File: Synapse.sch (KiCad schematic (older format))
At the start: 5 parts, among them U1 WeAct_BlackPill

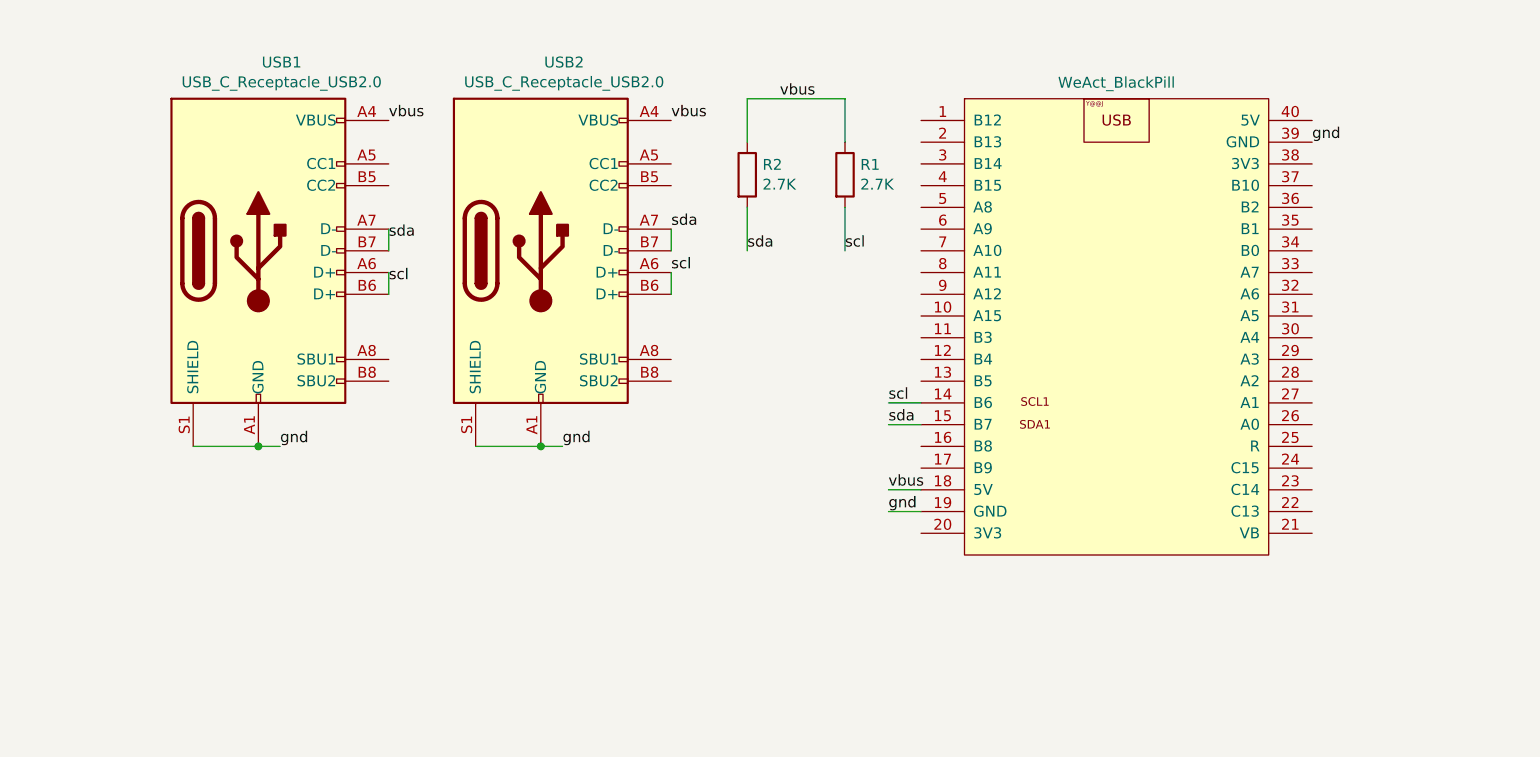
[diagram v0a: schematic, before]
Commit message: Rebuild the pcb in a cleaner way
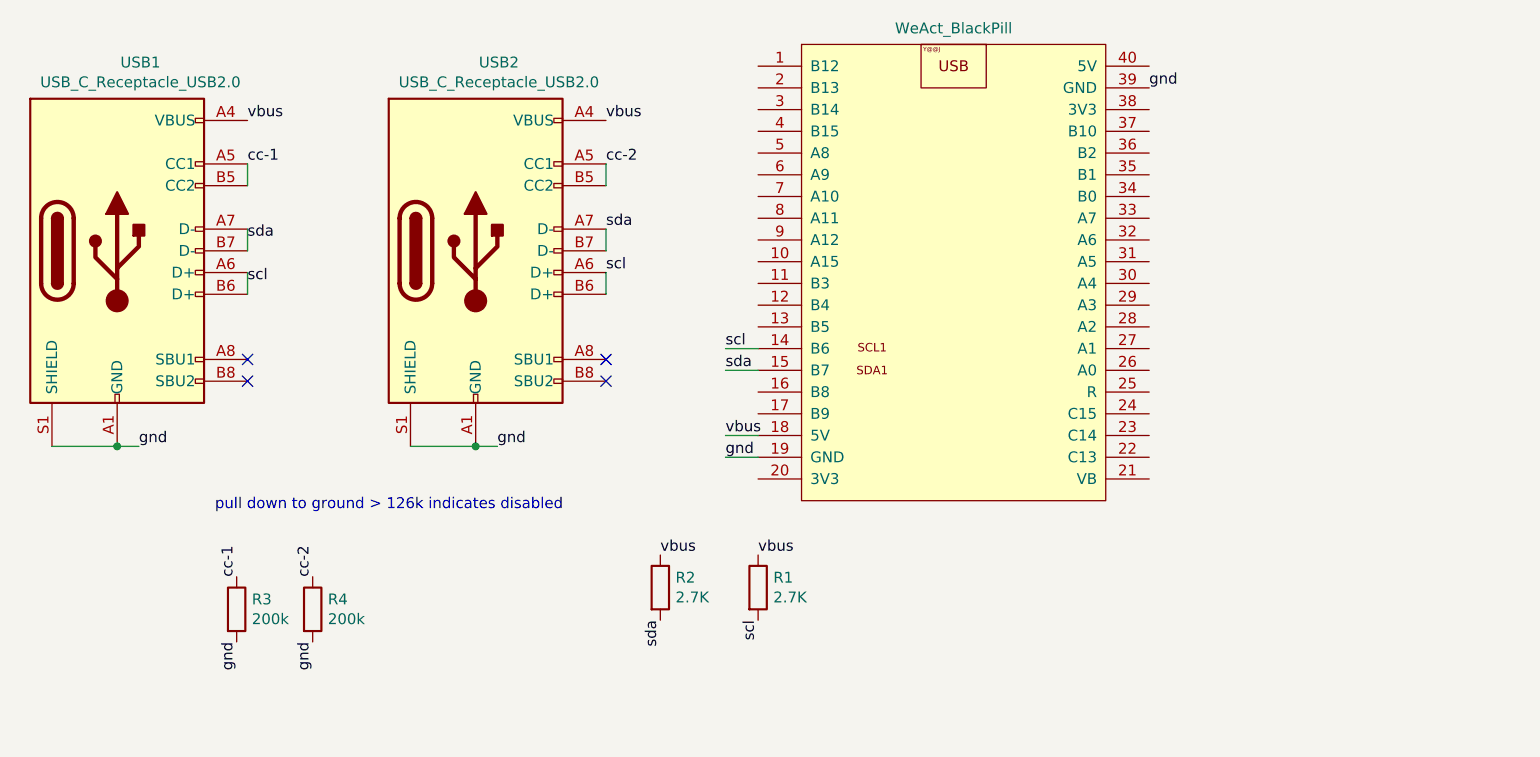
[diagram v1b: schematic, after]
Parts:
- added R3, R4: 200k, Resistor_SMD:R_1206_3216Metric, symbol Device:R
- R1, R2: LCSC (none) -> C17950
- USB1, USB2: LCSC (none) -> C165948
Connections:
- net gnd: now also R3.2, R4.2
- net cc-2: now reaches USB2.A5 (CC1)
- net cc-2: now also USB2.B5 (CC2), R4.1
- net cc-1: now reaches USB1.A5 (CC1)
- net cc-1: now also USB1.B5 (CC2), R3.1
- no-connect marks 0 -> 4
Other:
- note added: "pull down to ground > 126k indicates disabled"
- moved on the sheet: R1, R2, USB1, USB2
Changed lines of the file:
@@
 L Device:R R1
 U 1 1 60F04B0D
-P 6350 1850
-F 0 "R1" H 6420 1896 50  0000 L CNN
-F 1 "2.7K" H 6420 1805 50  0000 L CNN
-F 2 "Resistor_SMD:R_1206_3216Metric" V 6280 1850 50  0001 C CNN
-F 3 "~" H 6350 1850 50  0001 C CNN
-	1    6350 1850
-	1    0    0    -1
-$EndComp
-$Comp
-L Device:R R2
-U 1 1 60F0593A
-P 5900 1850
-F 0 "R2" H 5970 1896 50  0000 L CNN
-F 1 "2.7K" H 5970 1805 50  0000 L CNN
-F 2 "Resistor_SMD:R_1206_3216Metric" V 5830 1850 50  0001 C CNN
-F 3 "~" H 5900 1850 50  0001 C CNN
-	1    5900 1850
+P 5950 3750
+F 0 "R1" H 6020 3796 50  0000 L CNN
+F 1 "2.7K" H 6020 3705 50  0000 L CNN
+F 2 "Resistor_SMD:R_1206_3216Metric" V 5880 3750 50  0001 C CNN
+F 3 "~" H 5950 3750 50  0001 C CNN
+F 4 "C17950" H 5950 3750 50  0001 C CNN "LCSC"
+	1    5950 3750
 	1    0    0    -1
 $EndComp
 Wire Wire Line
-	6700 3400 6550 3400
+	5950 3150 5800 3150
 $Comp
 L Connector:USB_C_Receptacle_USB2.0 USB1
 U 1 1 60F0D514
-P 3650 2200
-F 0 "USB1" H 3757 3067 50  0000 C CNN
-F 1 "USB_C_Receptacle_USB2.0" H 3757 2976 50  0000 C CNN
-F 2 "Connector_USB:USB_C_Receptacle_HRO_TYPE-C-31-M-12" H 3800 2200 50  0001 C CNN
-F 3 "https://www.usb.org/sites/default/files/documents/usb_type-c.zip" H 3800 2200 50  0001 C CNN
-	1    3650 2200
+P 3000 2200
+F 0 "USB1" H 3107 3067 50  0000 C CNN
+F 1 "USB_C_Receptacle_USB2.0" H 3107 2976 50  0000 C CNN
+F 2 "Connector_USB:USB_C_Receptacle_HRO_TYPE-C-31-M-12" H 3150 2200 50  0001 C CNN
+F 3 "https://www.usb.org/sites/default/files/documents/usb_type-c.zip" H 3150 2200 50  0001 C CNN
+F 4 "C165948" H 3000 2200 50  0001 C CNN "LCSC"
+	1    3000 2200
 	1    0    0    -1
 $EndComp
 Wire Wire Line
-	5550 2100 5550 2200
+	5250 2100 5250 2200
 Wire Wire Line
-	4650 3100 4950 3100
-Connection ~ 4950 3100
+	4350 3100 4650 3100
+Connection ~ 4650 3100
 Wire Wire Line
-	3350 3100 3650 3100
-Text Label 6550 3400 0    50   ~ 0
+	2700 3100 3000 3100
+Text Label 5800 3150 0    50   ~ 0
 gnd
-Text Label 6550 3300 0    50   ~ 0
+Text Label 5800 3050 0    50   ~ 0
 vbus
-Text Label 8500 1700 0    50   ~ 0
+Text Label 7750 1450 0    50   ~ 0
 gnd
-Text Label 5550 2100 0    50   ~ 0
+Text Label 5250 2100 0    50   ~ 0
 sda
-Text Label 6550 3000 0    50   ~ 0
+Text Label 5800 2750 0    50   ~ 0
 sda
-Text Label 6050 1500 0    50   ~ 0
+Text Label 5250 1600 0    50   ~ 0
 vbus
+Text Label 5950 3900 3    50   ~ 0
+scl
+Text Label 5800 2650 0    50   ~ 0
+scl
 Wire Wire Line
-	5900 1500 5900 1700
+	5800 2650 5950 2650
 Wire Wire Line
-	6350 1500 6350 1700
+	5800 3050 5950 3050
+Text Label 4750 3100 0    50   ~ 0
+gnd
 Wire Wire Line
-	5900 1500 6350 1500
-Text Label 5550 1600 0    50   ~ 0
-vbus
-Text Label 5900 2200 0    50   ~ 0
+	4650 3100 4750 3100
+Text Label 3100 3100 0    50   ~ 0
+gnd
+Wire Wire Line
+	3000 3100 3100 3100
+Connection ~ 3000 3100
+Text Label 3600 2150 0    50   ~ 0
 sda
 Wire Wire Line
-	5900 2200 5900 2000
-Text Label 6350 2200 0    50   ~ 0
+	3600 2100 3600 2200
+Wire Wire Line
+	5950 2750 5800 2750
+Text Label 3600 2350 0    50   ~ 0
 scl
 Wire Wire Line
-	6350 2200 6350 2000
-Text Label 6550 2900 0    50   ~ 0
+	3600 2300 3600 2400
+Text Label 5250 2300 0    50   ~ 0
 scl
-Wire Wire Line
-	6550 2900 6700 2900
-Wire Wire Line
-	6550 3300 6700 3300
-Text Label 5050 3100 0    50   ~ 0
-gnd
-Wire Wire Line
-	4950 3100 5050 3100
-Text Label 3750 3100 0    50   ~ 0
-gnd
-Wire Wire Line
-	3650 3100 3750 3100
-Connection ~ 3650 3100
-Text Label 4250 2150 0    50   ~ 0
-sda
-Wire Wire Line
-	4250 2100 4250 2200
-Wire Wire Line
-	6700 3000 6550 3000
-Text Label 4250 2350 0    50   ~ 0
-scl
-Wire Wire Line
-	4250 2300 4250 2400
-Text Label 5550 2300 0    50   ~ 0
-scl
-Text Label 4250 1600 0    50   ~ 0
+Text Label 3600 1600 0    50   ~ 0
 vbus
 $Comp
 L Connector:USB_C_Receptacle_USB2.0 USB2
 U 1 1 60F06A9E
-P 4950 2200
-F 0 "USB2" H 5057 3067 50  0000 C CNN
-F 1 "USB_C_Receptacle_USB2.0" H 5057 2976 50  0000 C CNN
-F 2 "Connector_USB:USB_C_Receptacle_HRO_TYPE-C-31-M-12" H 5100 2200 50  0001 C CNN
-F 3 "https://www.usb.org/sites/default/files/documents/usb_type-c.zip" H 5100 2200 50  0001 C CNN
-	1    4950 2200
+P 4650 2200
+F 0 "USB2" H 4757 3067 50  0000 C CNN
+F 1 "USB_C_Receptacle_USB2.0" H 4757 2976 50  0000 C CNN
+F 2 "Connector_USB:USB_C_Receptacle_HRO_TYPE-C-31-M-12" H 4800 2200 50  0001 C CNN
+F 3 "https://www.usb.org/sites/default/files/documents/usb_type-c.zip" H 4800 2200 50  0001 C CNN
+F 4 "C165948" H 4650 2200 50  0001 C CNN "LCSC"
+	1    4650 2200
 	1    0    0    -1
 $EndComp
 Wire Wire Line
-	5550 2400 5550 2300
+	5250 2400 5250 2300
 $Comp
 L YAAJ_BlackPill:WeAct_BlackPill U1
 U 1 1 60EFFF91
-P 7600 2500
-F 0 "U1" H 7600 3665 50  0001 C CNN
-F 1 "WeAct_BlackPill" H 7600 3574 50  0000 C CNN
-F 2 "Footprints:YAAJ_BluePill_2" H 8400 1500 50  0001 C CNN
-F 3 "" H 8400 1500 50  0001 C CNN
-	1    7600 2500
+P 6850 2250
+F 0 "U1" H 6850 3415 50  0001 C CNN
+F 1 "WeAct_BlackPill" H 6850 3324 50  0000 C CNN
+F 2 "Footprints:YAAJ_BluePill_2" H 7650 1250 50  0001 C CNN
+F 3 "" H 7650 1250 50  0001 C CNN
+	1    6850 2250
 	1    0    0    -1
 $EndComp
+NoConn ~ 5250 2700
+NoConn ~ 5250 2800
+NoConn ~ 3600 2700
+NoConn ~ 3600 2800
+$Comp
+L Device:R R4
+U 1 1 60F1AE6D
+P 3900 3850
+F 0 "R4" H 3970 3896 50  0000 L CNN
+F 1 "200k" H 3970 3805 50  0000 L CNN
+F 2 "Resistor_SMD:R_1206_3216Metric" V 3830 3850 50  0001 C CNN
+F 3 "~" H 3900 3850 50  0001 C CNN
+F 4 "C17954" H 3900 3850 50  0001 C CNN "LCSC"
+	1    3900 3850
+	1    0    0    -1
+$EndComp
+Text Label 5950 3600 0    50   ~ 0
+vbus
+Text Label 5500 3900 3    50   ~ 0
+sda
+Text Label 5500 3600 0    50   ~ 0
+vbus
+$Comp
+L Device:R R2
+U 1 1 60F0593A
+P 5500 3750
+F 0 "R2" H 5570 3796 50  0000 L CNN
+F 1 "2.7K" H 5570 3705 50  0000 L CNN
+F 2 "Resistor_SMD:R_1206_3216Metric" V 5430 3750 50  0001 C CNN
+F 3 "~" H 5500 3750 50  0001 C CNN
+F 4 "C17950" H 5500 3750 50  0001 C CNN "LCSC"
+	1    5500 3750
+	1    0    0    -1
+$EndComp
+Text Label 3550 3700 1    50   ~ 0
+cc-1
+$Comp
+L Device:R R3
+U 1 1 60F1A5DE
+P 3550 3850
+F 0 "R3" H 3620 3896 50  0000 L CNN
+F 1 "200k" H 3620 3805 50  0000 L CNN
+F 2 "Resistor_SMD:R_1206_3216Metric" V 3480 3850 50  0001 C CNN
+F 3 "~" H 3550 3850 50  0001 C CNN
+F 4 "C17954" H 3550 3850 50  0001 C CNN "LCSC"
+	1    3550 3850
+	1    0    0    -1
+$EndComp
+Text Label 3900 3700 1    50   ~ 0
+cc-2
+Text Notes 3450 3400 0    50   ~ 0
+pull down to ground > 126k indicates disabled
+Text Label 3600 1800 0    50   ~ 0
+cc-1
+Wire Wire Line
+	3600 1800 3600 1900
+Text Label 5250 1800 0    50   ~ 0
+cc-2
+Wire Wire Line
+	5250 1800 5250 1900
+Text Label 3550 4000 3    50   ~ 0
+gnd
+Text Label 3900 4000 3    50   ~ 0
+gnd
 $EndSCHEMATC

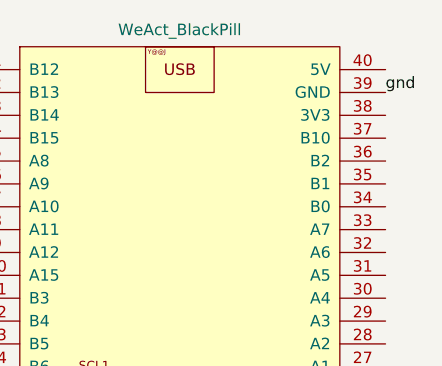
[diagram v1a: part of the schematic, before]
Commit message: Use VCC for a top layer
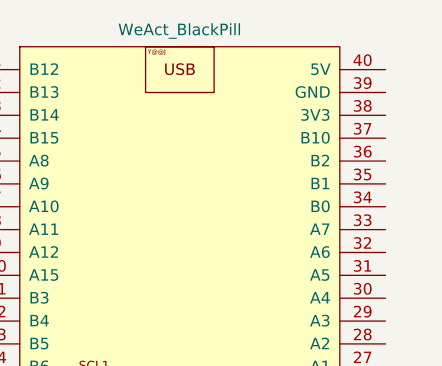
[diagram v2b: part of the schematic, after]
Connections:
- net gnd: no longer U1.39 (GND)
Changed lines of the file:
@@
 Text Label 5800 3050 0    50   ~ 0
 vbus
-Text Label 7750 1450 0    50   ~ 0
-gnd
 Text Label 5250 2100 0    50   ~ 0
 sda

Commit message: synapse mini
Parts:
- removed U1: WeAct_BlackPill, Footprints:YAAJ_BluePill_2, symbol YAAJ_BlackPill:WeAct_BlackPill
- added U2: WeAct_BlackPill_Short, Footprints:BlackPill_Short, symbol YAAJ_BlackPill:WeAct_BlackPill_Short
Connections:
- wire segments 14 -> 18
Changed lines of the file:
@@
 	1    0    0    -1
 $EndComp
-Wire Wire Line
-	5950 3150 5800 3150
 $Comp
 L Connector:USB_C_Receptacle_USB2.0 USB1
@@
 Wire Wire Line
 	2700 3100 3000 3100
-Text Label 5800 3150 0    50   ~ 0
+Text Label 5750 2150 2    50   ~ 0
 gnd
-Text Label 5800 3050 0    50   ~ 0
+Text Label 5750 2050 2    50   ~ 0
 vbus
 Text Label 5250 2100 0    50   ~ 0
 sda
-Text Label 5800 2750 0    50   ~ 0
+Text Label 5750 1750 2    50   ~ 0
 sda
 Text Label 5250 1600 0    50   ~ 0
@@
 Text Label 5950 3900 3    50   ~ 0
 scl
-Text Label 5800 2650 0    50   ~ 0
+Text Label 5750 1650 2    50   ~ 0
 scl
-Wire Wire Line
-	5800 2650 5950 2650
-Wire Wire Line
-	5800 3050 5950 3050
 Text Label 4750 3100 0    50   ~ 0
 gnd
@@
 Wire Wire Line
 	3600 2100 3600 2200
-Wire Wire Line
-	5950 2750 5800 2750
 Text Label 3600 2350 0    50   ~ 0
 scl
@@
 Wire Wire Line
 	5250 2400 5250 2300
-$Comp
-L YAAJ_BlackPill:WeAct_BlackPill U1
-U 1 1 60EFFF91
-P 6850 2250
-F 0 "U1" H 6850 3415 50  0001 C CNN
-F 1 "WeAct_BlackPill" H 6850 3324 50  0000 C CNN
-F 2 "Footprints:YAAJ_BluePill_2" H 7650 1250 50  0001 C CNN
-F 3 "" H 7650 1250 50  0001 C CNN
-	1    6850 2250
-	1    0    0    -1
-$EndComp
 NoConn ~ 5250 2700
 NoConn ~ 5250 2800
@@
 Text Label 3900 4000 3    50   ~ 0
 gnd
+$Comp
+L YAAJ_BlackPill:WeAct_BlackPill_Short U2
+U 1 1 60F02FCD
+P 6700 1950
+F 0 "U2" H 6700 2565 50  0000 C CNN
+F 1 "WeAct_BlackPill_Short" H 6700 2474 50  0000 C CNN
+F 2 "Footprints:BlackPill_Short" H 7500 1630 50  0001 C CNN
+F 3 "" H 7500 1630 50  0001 C CNN
+	1    6700 1950
+	1    0    0    -1
+$EndComp
+Wire Wire Line
+	5800 1650 5790 1650
+Connection ~ 5790 1650
+Wire Wire Line
+	5790 1650 5750 1650
+Wire Wire Line
+	5800 1750 5790 1750
+Connection ~ 5790 1750
+Wire Wire Line
+	5790 1750 5750 1750
+Wire Wire Line
+	5800 2050 5790 2050
+Connection ~ 5790 2050
+Wire Wire Line
+	5790 2050 5750 2050
+Wire Wire Line
+	5800 2150 5790 2150
+Connection ~ 5790 2150
+Wire Wire Line
+	5790 2150 5750 2150
 $EndSCHEMATC
